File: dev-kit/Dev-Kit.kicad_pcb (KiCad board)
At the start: 4 copper layers, 41 x 38 mm, 76 parts, among them IC101 nPM1300-QEXX, IC201 APDS-9306-065, IC202 BMI270, IC203 BMP581, IC204 LIS2MDLTR, IC302 FAN5622SX, IC303 MX25U51245GZ4I00, IC305 NTS0104GU12, IC306 DRV2603RUNT, IC307 RV-8263-C8, M301 NORA-B106, Q201 DMG1013UW-7, Q301 BC817W, Q302 PMZ550UNEYL, Q303 PMZ550UNEYL, X101 BATTERY, X302 GC9A01A_CST816S, X303 M+, X304 M-

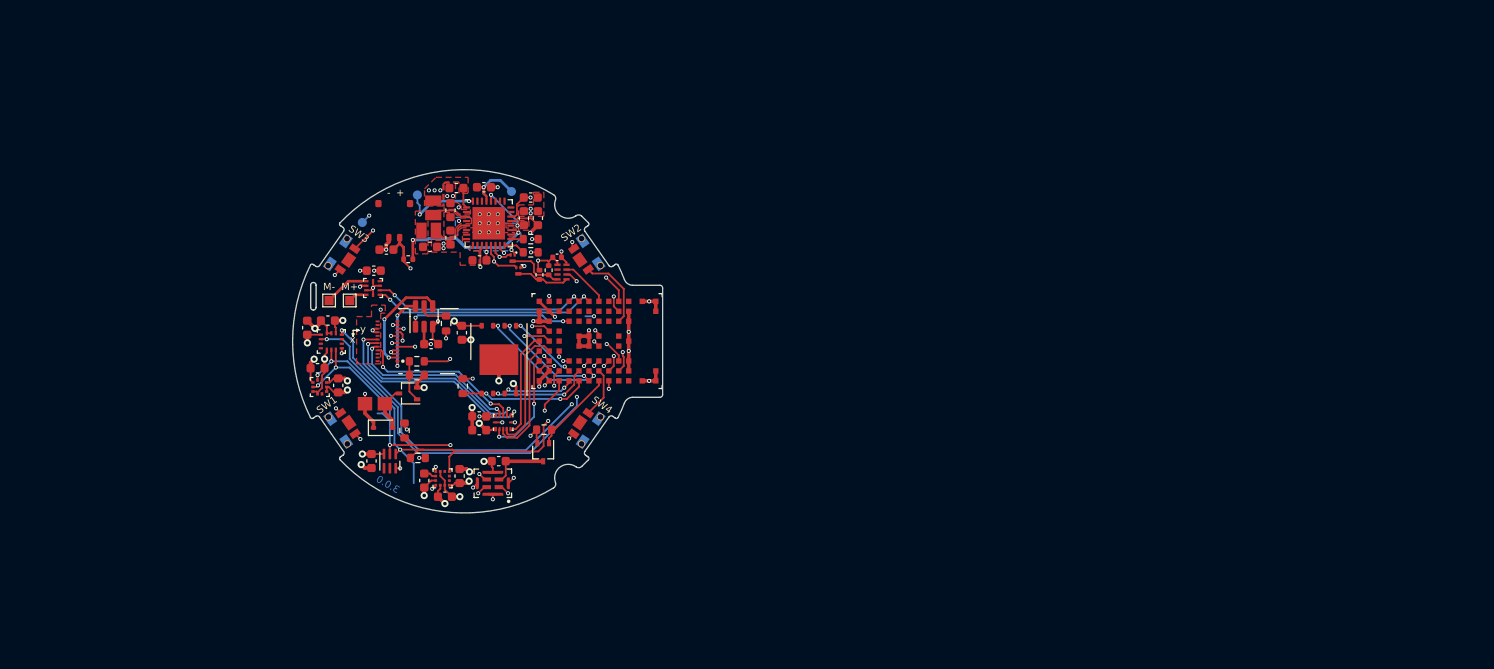
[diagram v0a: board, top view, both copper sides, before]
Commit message: Working on the layout for the dev kit
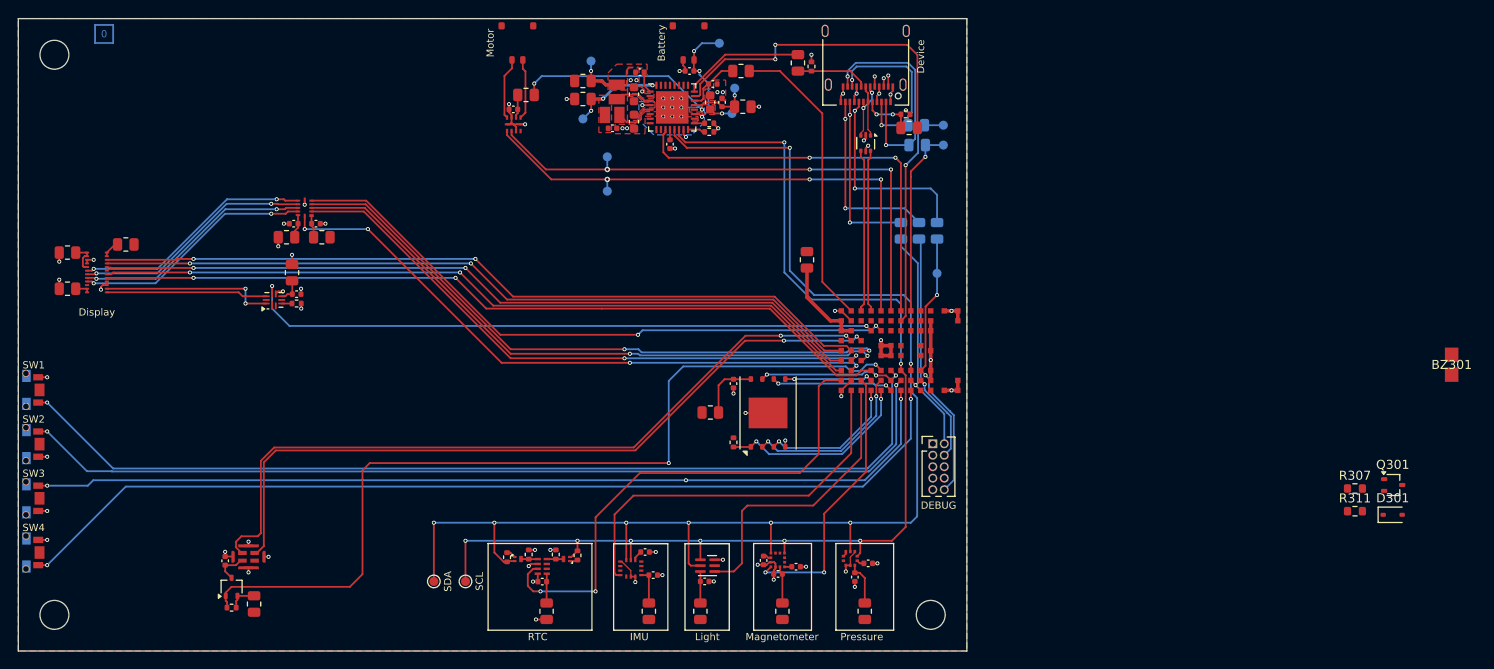
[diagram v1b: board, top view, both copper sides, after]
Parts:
- removed C108: 10u, Capacitor_SMD:C_0603_1608Metric
- removed G*** (x2): LOGO, LOGO
- removed G***: LOGO, project:Logo
- removed X303: M+, TestPoint:TestPoint_Pad_1.0x1.0mm
- removed X304: M-, TestPoint:TestPoint_Pad_1.0x1.0mm
- removed kibuzzard-656642B5: G***, kibuzzard-656642B5
- removed kibuzzard-656642E4: G***, kibuzzard-656642E4
- removed kibuzzard-65664337: G***, kibuzzard-65664337
- removed kibuzzard-65664342: G***, kibuzzard-65664342
- removed kibuzzard-6616D313: G***, kibuzzard-6616D313
- added IC107: USBLC6-2P6, Package_TO_SOT_SMD:SOT-666, F.Cu at (203.8, 90.8)
- added R104: 0R, Resistor_SMD:R_0805_2012Metric, F.Cu at (196.3, 81.9)
- added R105: 0R, Resistor_SMD:R_0805_2012Metric, F.Cu at (208.6, 89.1)
- added R106: 0R, Resistor_SMD:R_0805_2012Metric, B.Cu at (207.7, 100.5)
- added R107: 0R, Resistor_SMD:R_0805_2012Metric, B.Cu at (209.7, 100.5)
- added R108: 0R, Resistor_SMD:R_0805_2012Metric, F.Cu at (172.5, 85.9)
- added R109: 0R, Resistor_SMD:R_0805_2012Metric, F.Cu at (190.0, 82.8)
- added R110: 0R, Resistor_SMD:R_0805_2012Metric, F.Cu at (197.3, 103.7)
- added R111: 5k1, Resistor_SMD:R_0402_1005Metric, F.Cu at (208.2, 87.6)
- added R112: 5k1, Resistor_SMD:R_0402_1005Metric, F.Cu at (197.8, 82.3)
- added R113: 0R, Resistor_SMD:R_0805_2012Metric, F.Cu at (121.9, 102.0)
- added R114: 0R, Resistor_SMD:R_0805_2012Metric, F.Cu at (115.4, 102.9)
- added R115: 0R, Resistor_SMD:R_0805_2012Metric, F.Cu at (115.4, 106.9)
- added R116: 0R, Resistor_SMD:R_0805_2012Metric, F.Cu at (185.5, 142.6)
- added R117: 0R, Resistor_SMD:R_0805_2012Metric, F.Cu at (143.6, 101.2)
- added R118: 0R, Resistor_SMD:R_0805_2012Metric, F.Cu at (139.7, 101.2)
- added R119: 0R, Resistor_SMD:R_0805_2012Metric, F.Cu at (190.2, 86.7)
- added R120: 0R, Resistor_SMD:R_0805_2012Metric, F.Cu at (168.5, 142.6)
- added R121: 0R, Resistor_SMD:R_0805_2012Metric, F.Cu at (166.2, 85.5)
- added R122: 0R, Resistor_SMD:R_0805_2012Metric, F.Cu at (136.1, 141.8)
- added R123: 0R, Resistor_SMD:R_0805_2012Metric, F.Cu at (194.6, 142.6)
- added R124: 0R, Resistor_SMD:R_0805_2012Metric, F.Cu at (203.7, 142.6)
- added R125: 0R, Resistor_SMD:R_0805_2012Metric, F.Cu at (179.8, 142.6)
- added R126: 0R, Resistor_SMD:R_0805_2012Metric, F.Cu at (140.3, 105.1)
- added R127: 0R, Resistor_SMD:R_0805_2012Metric, F.Cu at (186.6, 120.6)
- added R128: 0R, Resistor_SMD:R_0805_2012Metric, B.Cu at (209.5, 91.0)
- added R129: 0R, Resistor_SMD:R_0805_2012Metric, B.Cu at (209.4, 88.8)
- added R130: 0R, Resistor_SMD:R_0805_2012Metric, B.Cu at (211.7, 100.5)
- added REF**: MountingHole_3.2mm_M3, MountingHole:MountingHole_3.2mm_M3, F.Cu at (114.0, 81.0)
- added REF**: MountingHole_3.2mm_M3, MountingHole:MountingHole_3.2mm_M3, F.Cu at (114.0, 143.0)
- added REF**: MountingHole_3.2mm_M3, MountingHole:MountingHole_3.2mm_M3, F.Cu at (211.0, 143.0)
- added TP104: SDA, TestPoint:TestPoint_Pad_D1.0mm, F.Cu at (156.0, 139.3)
- added TP105: SCL, TestPoint:TestPoint_Pad_D1.0mm, F.Cu at (159.5, 139.3)
- added TP106: VSYS, TestPoint:TestPoint_Pad_D1.0mm, B.Cu at (189.0, 87.5)
- added TP107: VBAT, TestPoint:TestPoint_Pad_D1.0mm, B.Cu at (187.6, 79.7)
- added TP108: TxD, TestPoint:TestPoint_Pad_D1.0mm, B.Cu at (212.4, 88.8)
- added TP109: RxD, TestPoint:TestPoint_Pad_D1.0mm, B.Cu at (212.4, 91.0)
- added TP110: MCU Reset, TestPoint:TestPoint_Pad_D1.0mm, B.Cu at (211.7, 105.2)
- added TP111: VIB-PWM, TestPoint:TestPoint_Pad_D1.0mm, B.Cu at (175.2, 92.3)
- added TP112: VIB-EN, TestPoint:TestPoint_Pad_D1.0mm, B.Cu at (175.2, 96.1)
- added X102: Motor, Molex:78171-0002, F.Cu at (165.2, 79.7)
- added X103: Device, Connector_USB:USB_C_Receptacle_Amphenol_12401610E4-2A, F.Cu at (203.8, 81.2)
- added X104: DEBUG, Connector_PinHeader_1.27mm:PinHeader_2x05_P1.27mm_Vertical, F.Cu at (211.2, 124.1)
- C101, C102, C103, C105, C107, C110, C201, C202, C203, C204, C206, C207, C208, C209, C211, C301, C302, C304, C305, C306: footprint Capacitor_SMD:C_0603_1608Metric -> Capacitor_SMD:C_0402_1005Metric
- IC302: footprint Package_TO_SOT_SMD:TSOT-23-6 -> Package_DFN_QFN:UQFN-10_1.4x1.8mm_P0.4mm
- R101, R102, R201, R301, R302: footprint Resistor_SMD:R_0603_1608Metric -> Resistor_SMD:R_0402_1005Metric
- R103: footprint Resistor_SMD:R_0402_1005Metric -> Resistor_SMD:R_0805_2012Metric
- R303, R304: value 4k7 -> 1k8; footprint Resistor_SMD:R_0603_1608Metric -> Resistor_SMD:R_0402_1005Metric
- TP103: value 3V3 -> VBUS-In
- X101: value BATTERY -> Battery
- X302: value GC9A01A_CST816S -> Display
- moved BZ301 119.3 mm to (268.7, 115.3), turned to 0 degrees
- moved D301 112.2 mm to (262.1, 131.9)
- moved Q301 109.5 mm to (262.2, 128.6), turned to 0 degrees
- moved R311 105.2 mm to (258.0, 131.5), turned to 0 degrees
- moved R307 104.6 mm to (258.0, 129.0), turned to 0 degrees
- moved S302 66.0 mm to (110.9, 124.1), turned to -90 degrees
- moved S304 63.9 mm to (110.9, 136.1), turned to -90 degrees
- moved C207 63.8 mm to (202.6, 138.8), turned to -90 degrees
- moved C206 61.9 mm to (204.1, 137.3), turned to 180 degrees
- moved IC203 61.7 mm to (202.1, 136.8), turned to -90 degrees
- moved C203 47.1 mm to (180.3, 138.6), turned to 180 degrees
- moved S303 43.9 mm to (110.9, 130.1), turned to -90 degrees
- moved C202 43.5 mm to (179.4, 136.0), turned to 0 degrees
- moved IC202 41.6 mm to (177.8, 137.8), turned to 0 degrees
- moved R201 39.8 mm to (133.6, 142.2), turned to 0 degrees
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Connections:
- C101 pad 1: VBUS -> Net-(IC101-VBUS)
- C103 pad 1: /MCU/VBAT -> /Peripherals/VBAT
- C104 pad 1: /MCU/VSYS -> /Peripherals/VSYS
- C105 pad 1: +3V0 -> Net-(IC101-VOUT2)
- C106 pad 1: /MCU/VSYS -> /Peripherals/VSYS
- C107 pad 1: +1V8 -> Net-(IC101-VOUT1)
- C109 pad 1: /MCU/VSYS -> /Peripherals/VSYS
- C110 pad 1: /MCU/VBUS-MCU -> Net-(IC101-VBUSOUT)
- C201 pad 1: +1V8 -> Net-(IC201-VDD)
- C203 pad 2: +1V8 -> Net-(IC202-VDD)
- C207 pad 1: +1V8 -> Net-(IC203-VDD)
- C211 pad 1: +1V8 -> Net-(IC204-VDD)
- C301 pad 2: /MCU/VDD-Display -> Net-(IC302-VIN)
- C302 pad 1: +1V8 -> GND
- C302 pad 2: GND -> Net-(IC303-VCC)
- C304 pad 1: +1V8 -> Net-(IC305-VCCA)
- C305 pad 1: /MCU/VDD-Display -> Net-(IC305-VCCB)
- C306 pad 1: /MCU/VSYS -> Net-(IC306-VDD)
- C307 pad 1: /MCU/VBAT -> Net-(IC307-VDD)
- IC101 pad 1: +1V8 -> Net-(IC101-VOUT1)
- IC101 pad 13: /MCU/SENSOR-SDA -> /MCU/SDA
- IC101 pad 14: /MCU/SENSOR-SCL -> /MCU/SCL
- IC101 pad 15: BTN-3 -> /MCU/SW3
- IC101 pad 19: Net-(IC101-VBAT) -> /Peripherals/VBAT
- IC101 pad 20: /MCU/VSYS -> /Peripherals/VSYS
- IC101 pad 21: VBUS -> Net-(IC101-VBUS)
- IC101 pad 22: /MCU/VBUS-MCU -> Net-(IC101-VBUSOUT)
- IC101 pad 23: unconnected-(IC101-CC1-Pad23) -> /MCU/CC1
- IC101 pad 24: unconnected-(IC101-CC2-Pad24) -> /MCU/CC2
- IC101 pad 28: /MCU/VSYS -> unconnected-(IC101-LSIN1/VINLDO1-Pad28)
- IC101 pad 29: /MCU/VDD-Display -> unconnected-(IC101-LSOUT1/VOUTLDO1-Pad29)
- IC101 pad 32: +3V0 -> Net-(IC101-VOUT2)
- IC101 pad 4: /MCU/VSYS -> /Peripherals/VSYS
- IC201 pad 1: /MCU/SENSOR-SCL -> /MCU/SCL
- IC201 pad 2: /MCU/SENSOR-SDA -> /MCU/SDA
- IC201 pad 3: +1V8 -> Net-(IC201-VDD)
- IC201 pad 4: unconnected-(IC201-INT-Pad4) -> /MCU/APDS-INT
- IC202 pad 13: /MCU/SENSOR-SCL -> /MCU/SCL
- IC202 pad 14: /MCU/SENSOR-SDA -> /MCU/SDA
- IC202 pad 4: /MCU/BMI270-INT1 -> /MCU/BMI270-INT
- IC202 pad 8: +1V8 -> Net-(IC202-VDD)
- IC202 pad 9: /MCU/BMI270-INT2 -> unconnected-(IC202-INT2-Pad9)
- IC203 pad 10: +1V8 -> Net-(IC203-VDD)
- IC203 pad 2: /MCU/SENSOR-SCL -> /MCU/SCL
- IC203 pad 4: /MCU/SENSOR-SDA -> /MCU/SDA
- IC204 pad 1: /MCU/SENSOR-SCL -> /MCU/SCL
- IC204 pad 4: /MCU/SENSOR-SDA -> /MCU/SDA
- IC204 pad 9: +1V8 -> Net-(IC204-VDD)
- IC302 pad 1: DISPLAY-BLK -> unconnected-(IC302-LED3-Pad1)
- IC302 pad 2: GND -> unconnected-(IC302-LED4-Pad2)
- IC302 pad 3: /MCU/VDD-Display -> Net-(IC302-ISET)
- IC302 pad 4: LEDK2 -> unconnected-(IC302-NC-Pad4)
- IC302 pad 5: Net-(IC302-ISET) -> Net-(IC302-VIN)
- IC302 pad 6: LEDK1 -> GND
- IC303 pad 8: +1V8 -> Net-(IC303-VCC)
- IC305 pad 1: +1V8 -> Net-(IC305-VCCA)
- IC305 pad 11: /MCU/VDD-Display -> Net-(IC305-VCCB)
- IC305 pad 2: TOUCH-SCL -> TOUCH-INT
- IC305 pad 3: TOUCH-INT -> TOUCH-SCL
- IC306 pad 1: VIB-EN -> /MCU/VIB-EN
- IC306 pad 2: VIB-PWM -> /MCU/VIB-PWM
- IC306 pad 7: /MCU/VSYS -> Net-(IC306-VDD)
- IC307 pad 3: nRTC-INT -> /MCU/~{RTC-INT}
- IC307 pad 5: /MCU/VBAT -> Net-(IC307-VDD)
- L101 pad 1: +3V0 -> Net-(IC101-VOUT2)
- L102 pad 1: +1V8 -> Net-(IC101-VOUT1)
- M301 pad A2: DISPLAY-CS -> /MCU/~{RTC-INT}
- M301 pad A3: TOUCH-SCL -> DISPLAY-DATA
- M301 pad A4: TOUCH-INT -> DISPLAY-CLK
- M301 pad A5: TOUCH-RST -> DISPLAY-CS
- M301 pad A7: +1V8 -> Net-(M301A-VDDH)
- M301 pad A8: +1V8 -> Net-(M301A-VDDH)
- M301 pad B1: DISPLAY-CLK -> /MCU/BMI270-INT
- M301 pad B3: DISPLAY-DC -> DISPLAY-EN
- M301 pad B4: TOUCH-SDA -> TOUCH-INT
- M301 pad B6: BUZZER -> /MCU/MIC-DATA
- M301 pad B7: +1V8 -> Net-(M301A-VDDH)
- M301 pad B9: /MCU/VBUS-MCU -> /MCU/USB-VBUS-Out
- M301 pad C1: /MCU/SENSOR-SDA -> /MCU/APDS-INT
- M301 pad C2: DISPLAY-DATA -> /MCU/LIS2MDL-INT
- M301 pad C4: DISPLAY-EN -> TOUCH-SCL
- M301 pad C5: unconnected-(M301B-P0.02/NFC1-PadC5) -> TOUCH-SDA
- M301 pad C6: unconnected-(M301B-P0.00/XL1-PadC6) -> /MCU/MIC-CLK
- M301 pad C9: USB-D_P -> USB-D+
- M301 pad D3: /MCU/SENSOR-SCL -> DISPLAY-DC
- M301 pad D9: USB-D_N -> USB-D-
- M301 pad E3: unconnected-(M301B-P0.21-PadE3) -> /MCU/MIC-EN
- M301 pad E7: unconnected-(M301B-P0.06/AIN2-PadE7) -> TOUCH-RST
- M301 pad E9: VIB-PWM -> /MCU/VIB-EN
- M301 pad F3: /MCU/MIC-CLK -> /MCU/SW1
- M301 pad F9: VIB-EN -> /MCU/VIB-PWM
- M301 pad G1: /MCU/MIC-EN -> /MCU/SW3
- M301 pad G2: BTN-4 -> /MCU/SW2
- M301 pad G3: /MCU/MIC-DATA -> /MCU/SCL
- M301 pad G4: /MCU/BMI270-INT2 -> unconnected-(M301C-P1.04-PadG4)
- M301 pad G5: /MCU/BMI270-INT1 -> unconnected-(M301C-P1.08-PadG5)
- M301 pad G8: unconnected-(M301C-P1.12-PadG8) -> TxD
- M301 pad G9: nRTC-INT -> /MCU/PMIC-INT
- M301 pad H1: /MCU/LIS2MDL-INT -> /MCU/SW4
- M301 pad H3: BTN-1 -> /MCU/SDA
- M301 pad H9: unconnected-(M301C-P1.11-PadH9) -> RxD
- M301 pad J7: BTN-2 -> unconnected-(M301C-P1.10-PadJ7)
- M301 pad J8: /MCU/PMIC-INT -> unconnected-(M301B-P0.28/AIN7-PadJ8)
- M301 pad J9: BTN-3 -> unconnected-(M301B-P0.31-PadJ9)
- Q201 pad 2: +1V8 -> Net-(Q201-S)
- Q302 pad 2: /MCU/SENSOR-SCL -> /MCU/SCL
- Q303 pad 2: /MCU/SENSOR-SDA -> /MCU/SDA
- R103 pad 1: /MCU/VBAT -> +1V8
- R103 pad 2: Net-(IC101-VBAT) -> Net-(IC101-VOUT1)
- R201 pad 2: +1V8 -> Net-(Q201-S)
- R303 pad 2: /MCU/SENSOR-SDA -> /MCU/SDA
- R304 pad 2: /MCU/SENSOR-SCL -> /MCU/SCL
- R309 pad 1: /MCU/VBAT -> /Peripherals/VBAT
- R313 pad 1: /MCU/VBAT -> /Peripherals/VBAT
- S301 pad 1: BTN-1 -> /MCU/SW1
- S302 pad 2: BTN-2 -> /MCU/SW2
- S303 pad 2: BTN-3 -> /MCU/SW3
- S304 pad 1: BTN-4 -> /MCU/SW4
- TP101 pad 1: +1V8 -> Net-(IC101-VOUT1)
- TP102 pad 1: +3V0 -> Net-(IC101-VOUT2)
- TP103 pad 1: /MCU/VDD-Display -> Net-(IC101-VBUS)
- X101 pad 1: /MCU/VBAT -> /Peripherals/VBAT
- X302 pad 11: +1V8 -> Net-(R113-Pad1)
- X302 pad 12: +1V8 -> Net-(R113-Pad1)
- X302 pad 13: /MCU/VDD-Display -> Net-(X302-CTP-VDD)
- X302 pad 14: /MCU/VDD-Display -> Net-(X302-CTP-VDD)
- X302 pad 17: /MCU/VDD-Display -> Net-(X302-CTP-VDD)
- X302 pad 20: Net-(IC305-B1) -> Net-(IC305-B2)
- X302 pad 21: Net-(IC305-B2) -> Net-(IC305-B1)
- X302 pad 23: /MCU/VDD-Display -> Net-(X302-LEDA1)
- X302 pad 24: /MCU/VDD-Display -> Net-(X302-LEDA1)
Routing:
- net /MCU/SDA: track 0.00 -> 150.1 mm, vias 0 -> 8
- net /MCU/SW3: track 0.00 -> 142.3 mm, vias 0 -> 4
- net /MCU/SCL: track 0.00 -> 129.9 mm, vias 0 -> 8
- net /MCU/SW4: track 0.00 -> 107.7 mm, vias 0 -> 2
- net /MCU/SW1: track 0.00 -> 107.2 mm, vias 0 -> 2
- net /MCU/SW2: track 0.00 -> 105.3 mm, vias 0 -> 2
- net /MCU/MIC-EN: track 9.39 -> 97.5 mm, vias 0 -> 2
- net /MCU/SENSOR-SCL: track 86.5 -> 0.00 mm, vias 6 -> 0
- net /MCU/SENSOR-SDA: track 80.3 -> 0.00 mm, vias 7 -> 0
- net DISPLAY-DC: track 18.1 -> 89.3 mm
- net DISPLAY-RST: track 17.4 -> 86.6 mm
- net DISPLAY-CLK: track 20.7 -> 85.6 mm
- net DISPLAY-CS: track 21.2 -> 85.3 mm
- net /MCU/MIC-DATA: track 20.4 -> 84.1 mm
- net DISPLAY-DATA: track 22.9 -> 85.9 mm
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- added copper zone on In2.Cu, net +3V0
- added copper zone on In2.Cu, net /MCU/USB-VBUS-In
- added copper zone on In2.Cu, net /Peripherals/VBAT
- added copper zone on B.Cu, net /Peripherals/VSYS
- added copper zone on F.Cu, net /Peripherals/VSYS
- added copper zone on In2.Cu, net GND
- added copper zone on F.Cu, net Net-(IC101-VOUT1)
- added copper zone on F.Cu, net Net-(IC101-VOUT2)
- removed copper zone on In2.Cu, net +1V8
- removed copper zone on F.Cu, net +3V0
- removed copper zone on F.Cu, net /MCU/VDD-Display
- removed copper zone on B.Cu, net /MCU/VSYS
- removed copper zone on F.Cu, net /MCU/VSYS
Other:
- board size 41 x 38 mm -> 105 x 70 mm
- board text added: "${REVISION}"
- board text added: "IMU"
- board text added: "Light"
- board text added: "Magnetometer"
- board text added: "Pressure"
- board text added: "RTC"
- board text removed: "+"
- board text removed: "-"
- board text removed: "3.0.${REVISION}"
- board text removed: "Designed with"
- board text removed: "x"
- board text removed: "y"

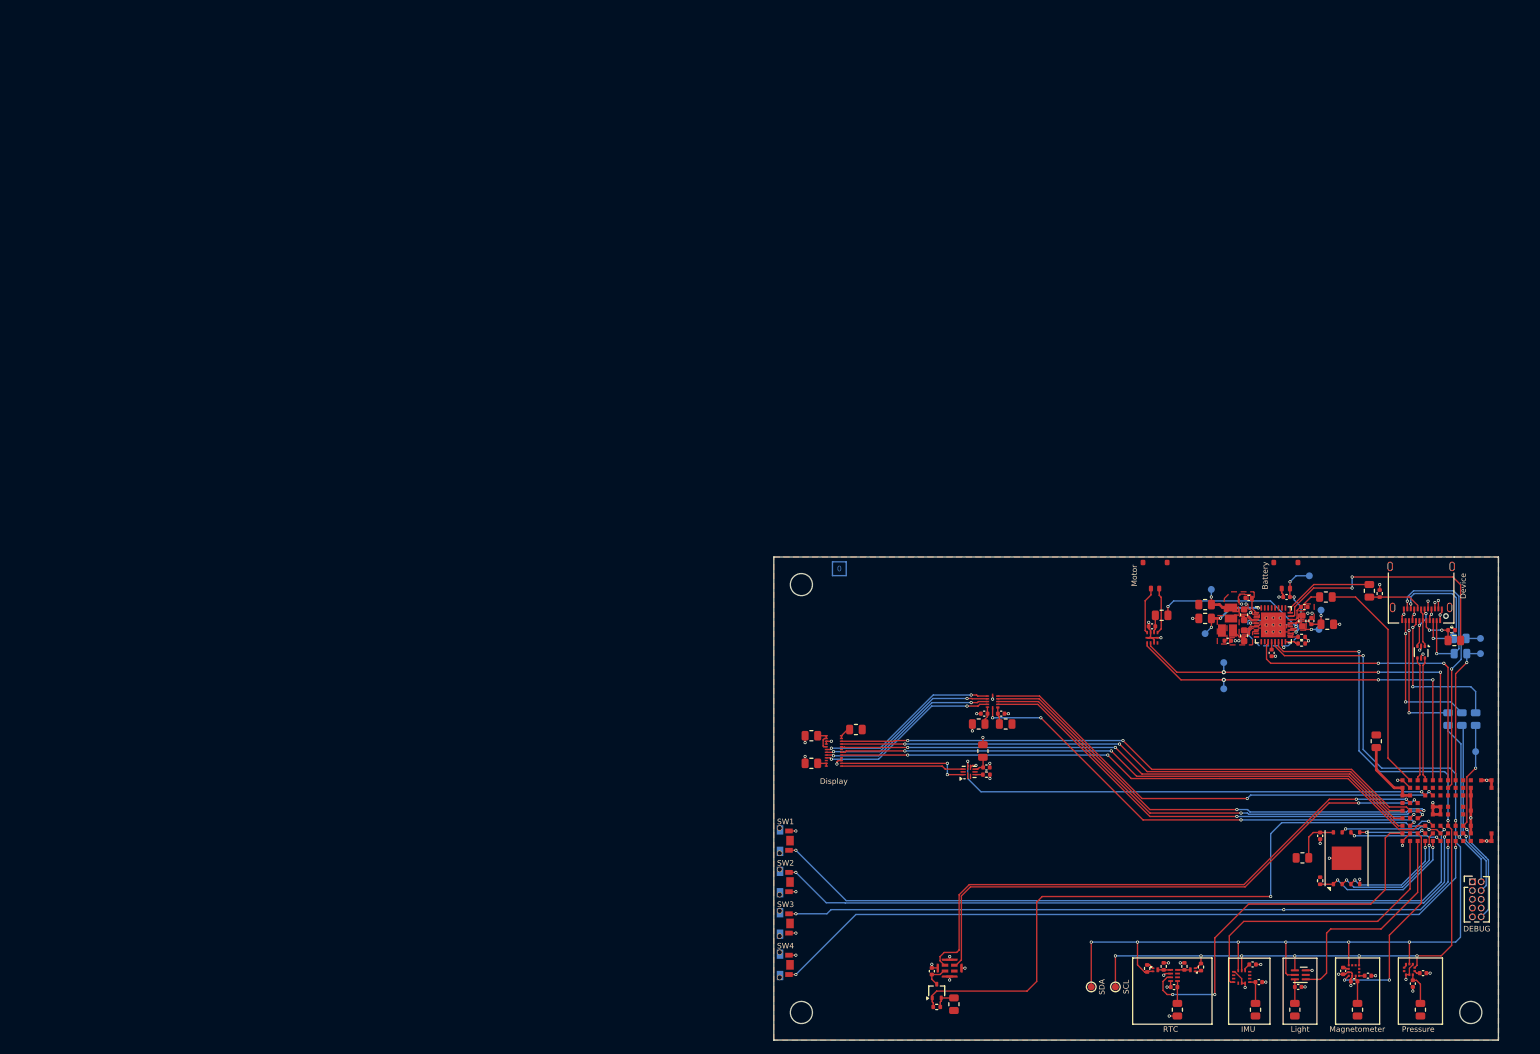
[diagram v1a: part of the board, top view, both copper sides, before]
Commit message: Add more documentation
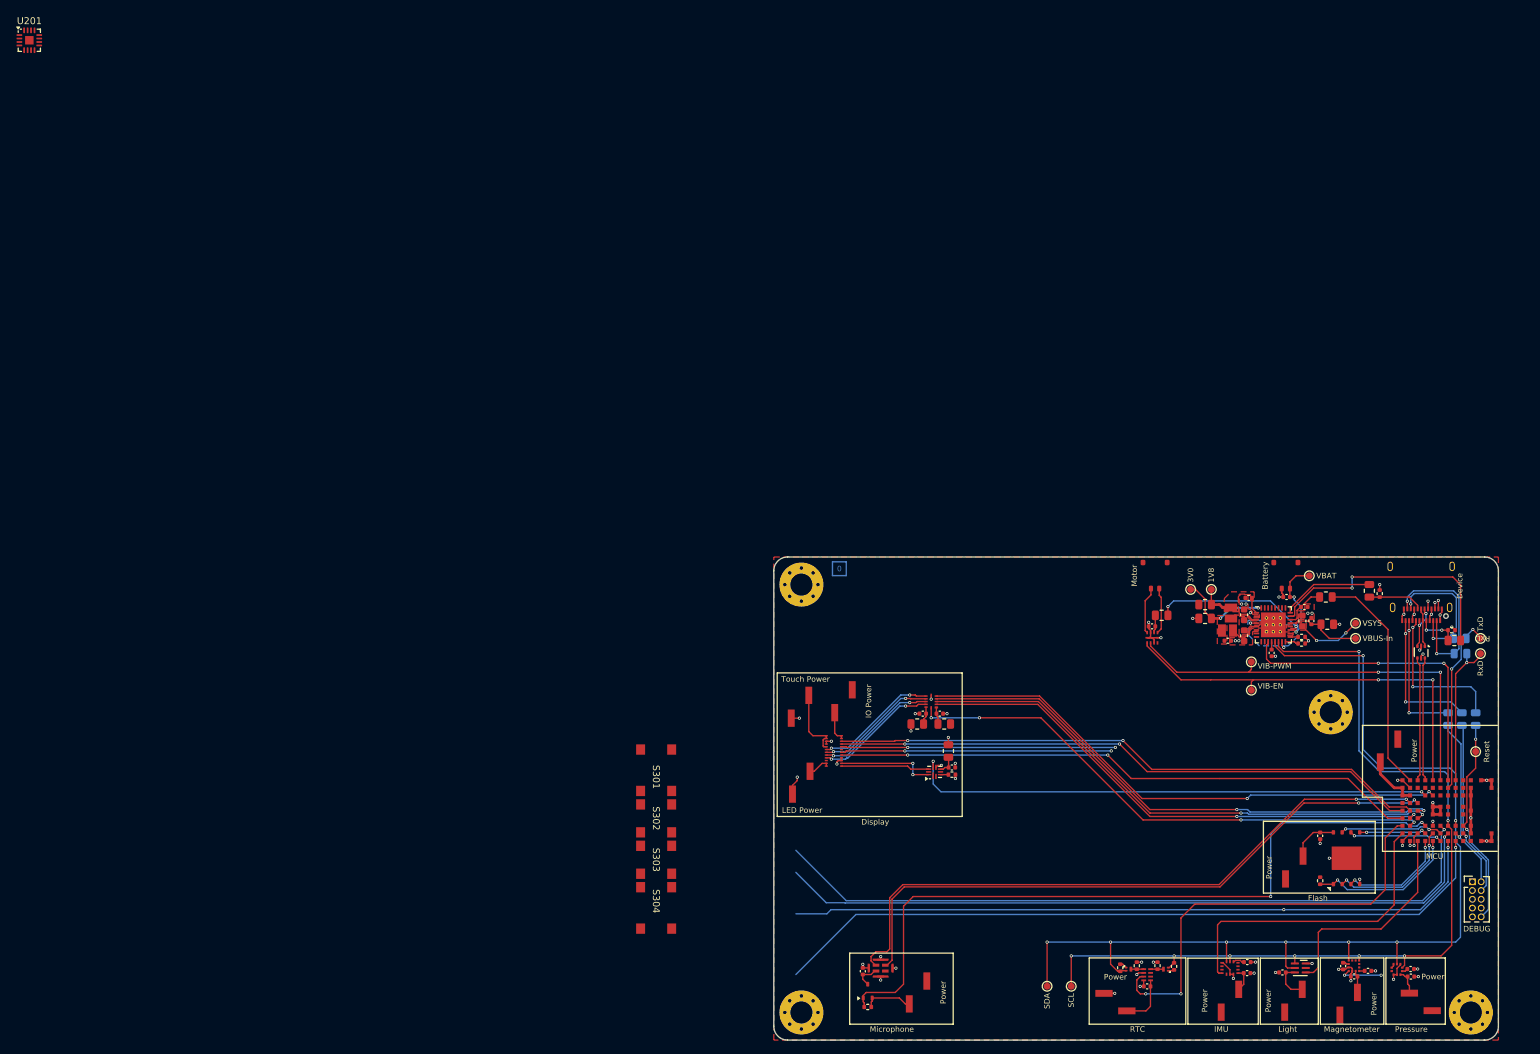
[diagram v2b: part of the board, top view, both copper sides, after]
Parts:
- removed R110, R113, R114, R115, R116, R120, R122, R123, R124, R125, R127: 0R, Resistor_SMD:R_0805_2012Metric
- added REF**: MountingHole_3.2mm_M3_Pad_Via, MountingHole:MountingHole_3.2mm_M3_Pad_Via, F.Cu at (190.7, 99.5)
- added U201: MAX98357A, Package_DFN_QFN:TQFN-16-1EP_3x3mm_P0.5mm_EP1.23x1.23mm, F.Cu at (2.12, 2.12)
- added X201: Power, Connector_PinHeader_2.54mm:PinHeader_1x02_P2.54mm_Vertical_SMD_Pin1Left, F.Cu at (130.9, 140.1)
- added X202: Power, Connector_PinHeader_2.54mm:PinHeader_1x02_P2.54mm_Vertical_SMD_Pin1Left, F.Cu at (203.8, 141.5)
- added X203: Power, Connector_PinHeader_2.54mm:PinHeader_1x02_P2.54mm_Vertical_SMD_Pin1Left, F.Cu at (193.3, 141.7)
- added X204: Power, Connector_PinHeader_2.54mm:PinHeader_1x02_P2.54mm_Vertical_SMD_Pin1Left, F.Cu at (185.3, 141.3)
- added X205: Power, Connector_PinHeader_2.54mm:PinHeader_1x02_P2.54mm_Vertical_SMD_Pin1Left, F.Cu at (176.1, 141.3)
- added X206: Power, Connector_PinHeader_2.54mm:PinHeader_1x02_P2.54mm_Vertical_SMD_Pin1Left, F.Cu at (159.5, 141.5)
- added X207: Power, Connector_PinHeader_2.54mm:PinHeader_1x02_P2.54mm_Vertical_SMD_Pin1Left, F.Cu at (199.2, 105.0)
- added X208: Power, Connector_PinHeader_2.54mm:PinHeader_1x02_P2.54mm_Vertical_SMD_Pin1Left, F.Cu at (185.4, 122.0)
- added X209: LED Power, Connector_PinHeader_2.54mm:PinHeader_1x02_P2.54mm_Vertical_SMD_Pin1Left, F.Cu at (114.0, 109.7)
- added X210: Touch Power, Connector_PinHeader_2.54mm:PinHeader_1x02_P2.54mm_Vertical_SMD_Pin1Left, F.Cu at (113.8, 98.7)
- added X211: IO Power, Connector_PinHeader_2.54mm:PinHeader_1x02_P2.54mm_Vertical_SMD_Pin1Left, F.Cu at (120.1, 97.9)
- REF** (x3): value MountingHole_3.2mm_M3 -> MountingHole_3.2mm_M3_Pad_Via; footprint MountingHole:MountingHole_3.2mm_M3 -> MountingHole:MountingHole_3.2mm_M3_Pad_Via
- S301, S302, S303, S304: footprint E-Switch:TL6340AF160Q_Modified -> Wuerth:WS-TASV-6x6
- TP101, TP102, TP103, TP106, TP107, TP108, TP109, TP111, TP112: moved to F.Cu
- TP110: value MCU Reset -> Reset; moved to F.Cu
- moved S301 20.2 mm to (93.0, 108.9)
- moved S302 20.2 mm to (93.0, 114.9)
- moved S303 20.2 mm to (93.0, 120.9)
- moved S304 20.2 mm to (93.0, 126.9)
- moved MK201 10.0 mm to (125.5, 136.6)
- moved Q201 10.0 mm to (123.6, 139.9)
- moved R201 10.0 mm to (123.6, 142.2)
- moved C204 10.0 mm to (122.9, 137.0)
- moved C305 8.90 mm to (131.6, 99.7)
- moved IC305 8.90 mm to (132.8, 98.0)
- moved R117 8.90 mm to (134.7, 101.2)
- moved R118 8.90 mm to (130.8, 101.2)
- moved C304 8.90 mm to (134.1, 99.7)
- moved TP102 6.74 mm to (170.4, 81.7)
- moved TP103 6.47 mm to (194.3, 88.8)
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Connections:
- M301 pad A2: /MCU/~{RTC-INT} -> /MCU/BMI270-INT
- M301 pad A3: DISPLAY-DATA -> /MCU/~{RTC-INT}
- M301 pad A4: DISPLAY-CLK -> DISPLAY-DC
- M301 pad B1: /MCU/BMI270-INT -> DISPLAY-DATA
- M301 pad C2: /MCU/LIS2MDL-INT -> DISPLAY-CLK
- M301 pad D3: DISPLAY-DC -> /MCU/MIC-EN
- M301 pad E3: /MCU/MIC-EN -> /MCU/LIS2MDL-INT
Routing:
- net /MCU/MIC-CLK: track 82.7 -> 92.5 mm
- net /MCU/MIC-DATA: track 84.1 -> 93.7 mm
- net Net-(IC305-B2): track 26.6 -> 17.7 mm
- net Net-(IC305-B4): track 26.7 -> 17.8 mm
- net TOUCH-SDA: track 69.7 -> 78.6 mm
- net TOUCH-SCL: track 69.6 -> 78.5 mm
- net TOUCH-RST: track 69.8 -> 78.7 mm
- net TOUCH-INT: track 67.9 -> 76.8 mm
- net DISPLAY-EN: track 69.6 -> 78.5 mm
- net Net-(IC305-B3): track 26.6 -> 17.7 mm
- net Net-(IC305-B1): track 26.7 -> 17.8 mm
- net /MCU/MIC-EN: track 97.5 -> 106.1 mm
- net /Peripherals/VSYS: track 25.2 -> 32.2 mm, vias 4 -> 5
- net Net-(X210-Pin_2): track 3.60 -> 10.4 mm
- net DISPLAY-CLK: track 85.6 -> 91.5 mm, vias 2 -> 3
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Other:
- outline, holes or cut-outs redrawn
- board text added: "Flash"
- board text added: "MCU"
- board text added: "Microphone"
- board text added: "RxD"
- board text added: "SWD"
- board text added: "TxD"
- board text added: "~{RESET}"
